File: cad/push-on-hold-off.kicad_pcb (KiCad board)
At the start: 2 copper layers, 22.9 x 12.7 mm, 11 parts, among them P1 CONN_01X04, P2 CONN_01X04, Q1 IRF7309IPBF, SW1 SW_PUSH_SMALL

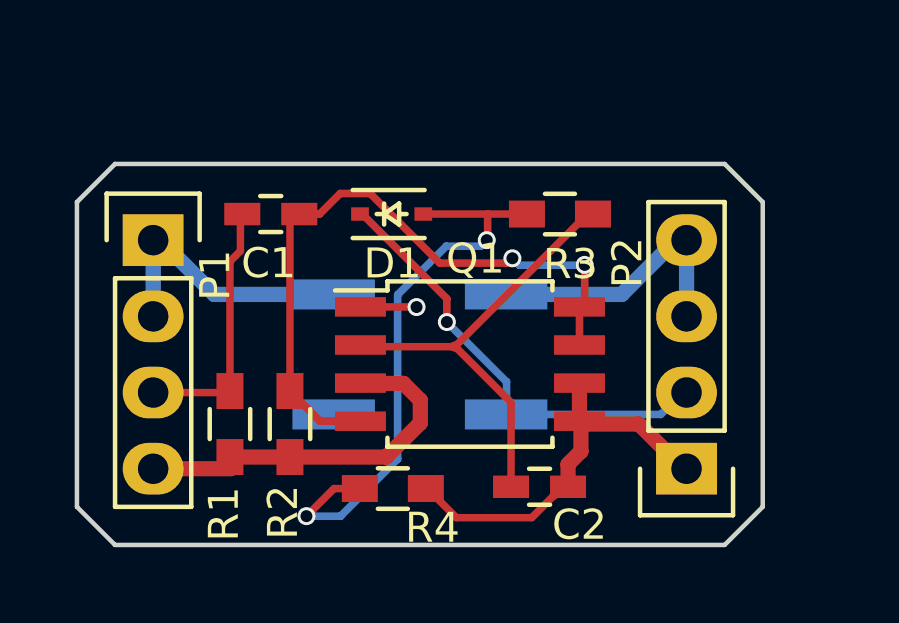
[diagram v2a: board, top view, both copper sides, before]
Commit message: Finish routing, add fills
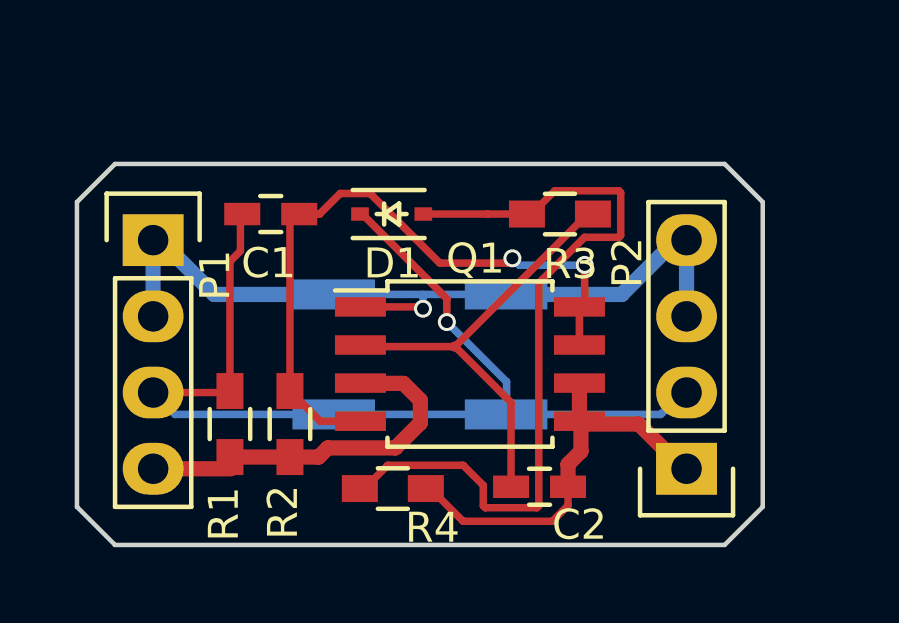
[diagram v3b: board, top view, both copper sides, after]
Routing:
- net /Button: track 23.9 -> 35.9 mm
- net Net-(D1-Pad2): track 19.7 -> 26.6 mm, vias 2 -> 0
- net GND: track 21.5 -> 28.0 mm
- net /Vout: track 13.4 -> 13.9 mm
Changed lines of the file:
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@@
   (general
     (links 27)
-    (no_connects 4)
+    (no_connects 0)
     (area 215.824999 100.254999 238.835001 113.105001)
     (thickness 1.6)
     (drawings 8)
-    (tracks 114)
+    (tracks 128)
     (zones 0)
     (modules 11)
@@
   )
   (setup
-    (last_trace_width 0.508)
+    (last_trace_width 0.25)
     (user_trace_width 0.508)
     (trace_clearance 0.2)
@@
   (segment (start 223 102.27) (end 223.38 101.89) (width 0.25) (layer F.Cu) (net 1))
   (segment (start 223.38 101.89) (end 223.31 102) (width 0.25) (layer F.Cu) (net 1))
+  (segment (start 224.455 108.68) (end 219.17 108.68) (width 0.25) (layer B.Cu) (net 2))
+  (segment (start 219.17 108.68) (end 218.44 107.95) (width 0.25) (layer B.Cu) (net 2))
+  (segment (start 230.205 108.68) (end 224.455 108.68) (width 0.25) (layer B.Cu) (net 2))
   (segment (start 230.205 108.68) (end 235.36 108.68) (width 0.254) (layer B.Cu) (net 2))
   (segment (start 235.36 108.68) (end 236.065 107.975) (width 0.254) (layer B.Cu) (net 2))
@@
   (segment (start 228.5 106.42) (end 225.51 106.42) (width 0.25) (layer F.Cu) (net 3))
   (segment (start 225.51 106.42) (end 225.35 106.365) (width 0.25) (layer F.Cu) (net 3))
+  (segment (start 232.27 111.715) (end 232.27 111.09) (width 0.25) (layer F.Cu) (net 4))
+  (segment (start 231.744988 112.240012) (end 232.27 111.715) (width 0.25) (layer F.Cu) (net 4))
+  (segment (start 227.68 111.15) (end 228.770012 112.240012) (width 0.25) (layer F.Cu) (net 4))
+  (segment (start 228.770012 112.240012) (end 231.744988 112.240012) (width 0.25) (layer F.Cu) (net 4))
+  (segment (start 227.53 111.15) (end 227.68 111.15) (width 0.25) (layer F.Cu) (net 4))
   (segment (start 232.27 111.09) (end 232.27 110.34) (width 0.508) (layer F.Cu) (net 4))
   (segment (start 232.27 110.34) (end 232.7 109.91) (width 0.508) (layer F.Cu) (net 4))
   (segment (start 232.7 109.91) (end 232.7 108.97) (width 0.508) (layer F.Cu) (net 4))
-  (segment (start 227.53 111.15) (end 227.58 111.15) (width 0.25) (layer F.Cu) (net 4))
-  (segment (start 227.58 111.15) (end 228.55 112.12) (width 0.25) (layer F.Cu) (net 4))
-  (segment (start 228.55 112.12) (end 231.06 112.12) (width 0.25) (layer F.Cu) (net 4))
-  (segment (start 231.06 112.12) (end 231.75 111.43) (width 0.25) (layer F.Cu) (net 4))
-  (segment (start 231.75 111.43) (end 232.27 111.09) (width 0.25) (layer F.Cu) (net 4))
   (segment (start 232.7 108.97) (end 232.65 108.905) (width 0.25) (layer F.Cu) (net 4))
   (segment (start 232.65 107.635) (end 232.65 108.94) (width 0.508) (layer F.Cu) (net 4))
@@
   (segment (start 234.63 109) (end 236.14 110.51) (width 0.508) (layer F.Cu) (net 4))
   (segment (start 236.14 110.51) (end 236.22 110.49) (width 0.25) (layer F.Cu) (net 4))
-  (segment (start 223.55 112.07) (end 224.69 112.07) (width 0.254) (layer B.Cu) (net 5))
-  (segment (start 229.59 102.84) (end 229.59 102) (width 0.254) (layer F.Cu) (net 5))
-  (segment (start 229.56 102.87) (end 229.59 102.84) (width 0.254) (layer F.Cu) (net 5))
-  (via (at 229.56 102.87) (size 0.6) (drill 0.4) (layers F.Cu B.Cu) (net 5))
-  (segment (start 229.36 103.07) (end 229.56 102.87) (width 0.254) (layer B.Cu) (net 5))
-  (segment (start 228.21 103.07) (end 229.36 103.07) (width 0.254) (layer B.Cu) (net 5))
-  (segment (start 226.59 104.69) (end 228.21 103.07) (width 0.254) (layer B.Cu) (net 5))
-  (segment (start 226.59 110.17) (end 226.59 104.69) (width 0.254) (layer B.Cu) (net 5))
-  (segment (start 224.69 112.07) (end 226.59 110.17) (width 0.254) (layer B.Cu) (net 5))
-  (segment (start 225.33 111.15) (end 224.47 111.15) (width 0.25) (layer F.Cu) (net 5))
-  (segment (start 223.55 112.07) (end 223.58 112.04) (width 0.25) (layer B.Cu) (net 5))
-  (via (at 223.55 112.07) (size 0.6) (drill 0.4) (layers F.Cu B.Cu) (net 5))
-  (segment (start 224.47 111.15) (end 223.55 112.07) (width 0.25) (layer F.Cu) (net 5))
+  (segment (start 225.33 111.15) (end 225.48 111.15) (width 0.25) (layer F.Cu) (net 5))
+  (segment (start 225.48 111.15) (end 226.255001 110.374999) (width 0.25) (layer F.Cu) (net 5))
+  (segment (start 233.960001 101.224999) (end 231.825001 101.224999) (width 0.25) (layer F.Cu) (net 5))
+  (segment (start 226.255001 110.374999) (end 228.774999 110.374999) (width 0.25) (layer F.Cu) (net 5))
+  (segment (start 228.774999 110.374999) (end 229.444999 111.044999) (width 0.25) (layer F.Cu) (net 5))
+  (segment (start 229.444999 111.725001) (end 229.509999 111.790001) (width 0.25) (layer F.Cu) (net 5))
+  (segment (start 229.444999 111.044999) (end 229.444999 111.725001) (width 0.25) (layer F.Cu) (net 5))
+  (segment (start 229.509999 111.790001) (end 231.230001 111.790001) (width 0.25) (layer F.Cu) (net 5))
+  (segment (start 231.230001 111.790001) (end 231.295001 111.725001) (width 0.25) (layer F.Cu) (net 5))
+  (segment (start 234.025001 101.289999) (end 233.960001 101.224999) (width 0.25) (layer F.Cu) (net 5))
+  (segment (start 231.295001 111.725001) (end 231.295001 104.299997) (width 0.25) (layer F.Cu) (net 5))
+  (segment (start 231.295001 104.299997) (end 232.819997 102.775001) (width 0.25) (layer F.Cu) (net 5))
+  (segment (start 232.819997 102.775001) (end 233.960001 102.775001) (width 0.25) (layer F.Cu) (net 5))
+  (segment (start 231.05 102) (end 230.9 102) (width 0.25) (layer F.Cu) (net 5))
+  (segment (start 233.960001 102.775001) (end 234.025001 102.710001) (width 0.25) (layer F.Cu) (net 5))
+  (segment (start 234.025001 102.710001) (end 234.025001 101.289999) (width 0.25) (layer F.Cu) (net 5))
+  (segment (start 231.825001 101.224999) (end 231.05 102) (width 0.25) (layer F.Cu) (net 5))
   (segment (start 227.445 102) (end 229.59 102) (width 0.25) (layer F.Cu) (net 5))
   (segment (start 229.59 102) (end 230.87 102) (width 0.25) (layer F.Cu) (net 5))
   (segment (start 230.87 102) (end 230.94 101.93) (width 0.25) (layer F.Cu) (net 5))
   (segment (start 230.94 101.93) (end 230.9 102) (width 0.25) (layer F.Cu) (net 5))
+  (segment (start 227.435 105.155) (end 227.435 104.705) (width 0.25) (layer B.Cu) (net 6))
+  (via (at 227.435 105.155) (size 0.6) (drill 0.4) (layers F.Cu B.Cu) (net 6))
+  (segment (start 225.35 105.095) (end 227.375 105.095) (width 0.25) (layer F.Cu) (net 6))
+  (segment (start 227.375 105.095) (end 227.435 105.155) (width 0.25) (layer F.Cu) (net 6))
+  (segment (start 227.425 104.695) (end 227.425 104.68) (width 0.25) (layer B.Cu) (net 6))
+  (segment (start 227.435 104.705) (end 227.425 104.695) (width 0.25) (layer B.Cu) (net 6))
+  (segment (start 224.455 104.68) (end 227.425 104.68) (width 0.25) (layer B.Cu) (net 6))
+  (segment (start 227.425 104.68) (end 230.205 104.68) (width 0.25) (layer B.Cu) (net 6))
   (segment (start 236.22 102.87) (end 236.22 105.52) (width 0.508) (layer B.Cu) (net 6))
   (segment (start 236.22 105.52) (end 236.26 105.56) (width 0.25) (layer B.Cu) (net 6))
@@
   (segment (start 220.48 104.68) (end 218.75 102.95) (width 0.508) (layer B.Cu) (net 6))
   (segment (start 218.75 102.95) (end 218.44 102.87) (width 0.25) (layer B.Cu) (net 6))
-  (segment (start 225.35 105.095) (end 227.215 105.095) (width 0.25) (layer F.Cu) (net 6))
-  (via (at 227.22 105.1) (size 0.6) (drill 0.4) (layers F.Cu B.Cu) (net 6))
-  (segment (start 227.215 105.095) (end 227.22 105.1) (width 0.25) (layer F.Cu) (net 6))
-  (segment (start 223 110.1) (end 226.21 110.1) (width 0.508) (layer F.Cu) (net 7))
+  (segment (start 227.345 108.965) (end 227.345 108.205) (width 0.508) (layer F.Cu) (net 7))
   (segment (start 226.785 107.645) (end 225.345 107.645) (width 0.508) (layer F.Cu) (net 7))
+  (segment (start 224.262012 109.795988) (end 226.514012 109.795988) (width 0.508) (layer F.Cu) (net 7))
+  (segment (start 226.514012 109.795988) (end 227.345 108.965) (width 0.508) (layer F.Cu) (net 7))
+  (segment (start 223.958 110.1) (end 224.262012 109.795988) (width 0.508) (layer F.Cu) (net 7))
+  (segment (start 223 110.1) (end 223.958 110.1) (width 0.508) (layer F.Cu) (net 7))
   (segment (start 227.345 108.205) (end 226.785 107.645) (width 0.508) (layer F.Cu) (net 7))
-  (segment (start 227.345 108.965) (end 227.345 108.205) (width 0.508) (layer F.Cu) (net 7))
-  (segment (start 226.21 110.1) (end 227.345 108.965) (width 0.508) (layer F.Cu) (net 7))
   (segment (start 225.345 107.645) (end 225.35 107.635) (width 0.254) (layer F.Cu) (net 7))
   (segment (start 223 110.1) (end 223 110.07) (width 0.25) (layer F.Cu) (net 7))
@@
     (connect_pads (clearance 0.508))
     (min_thickness 0.254)
-    (fill (arc_segments 16) (thermal_gap 0.508) (thermal_bridge_width 0.508))
+    (fill yes (arc_segments 16) (thermal_gap 0.508) (thermal_bridge_width 0.508))
     (polygon
       (pts
@@
     (connect_pads (clearance 0.508))
     (min_thickness 0.254)
-    (fill (arc_segments 16) (thermal_gap 0.508) (thermal_bridge_width 0.508))
+    (fill yes (arc_segments 16) (thermal_gap 0.508) (thermal_bridge_width 0.508))
     (polygon
       (pts
